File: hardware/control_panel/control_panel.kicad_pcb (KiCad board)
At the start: 2 copper layers, 70 x 37 mm, 12 parts

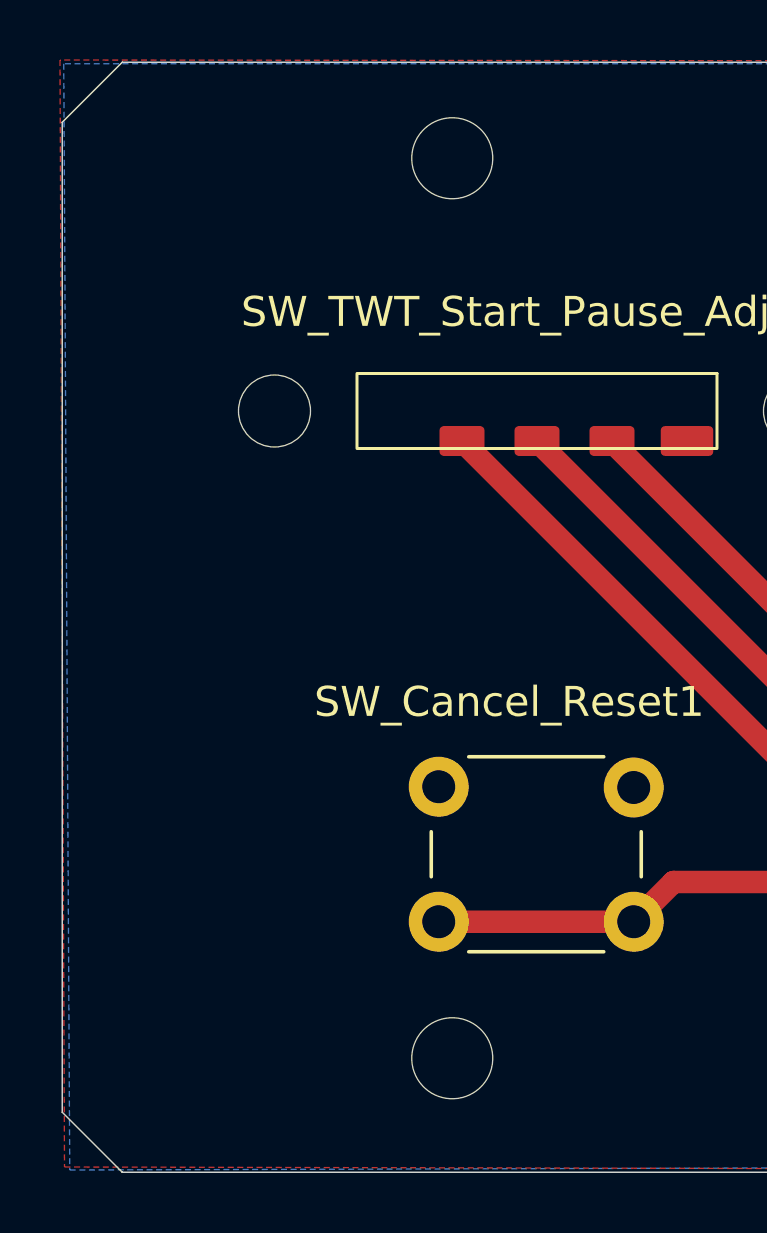
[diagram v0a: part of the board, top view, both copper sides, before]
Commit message: KiCad changes for mountholes
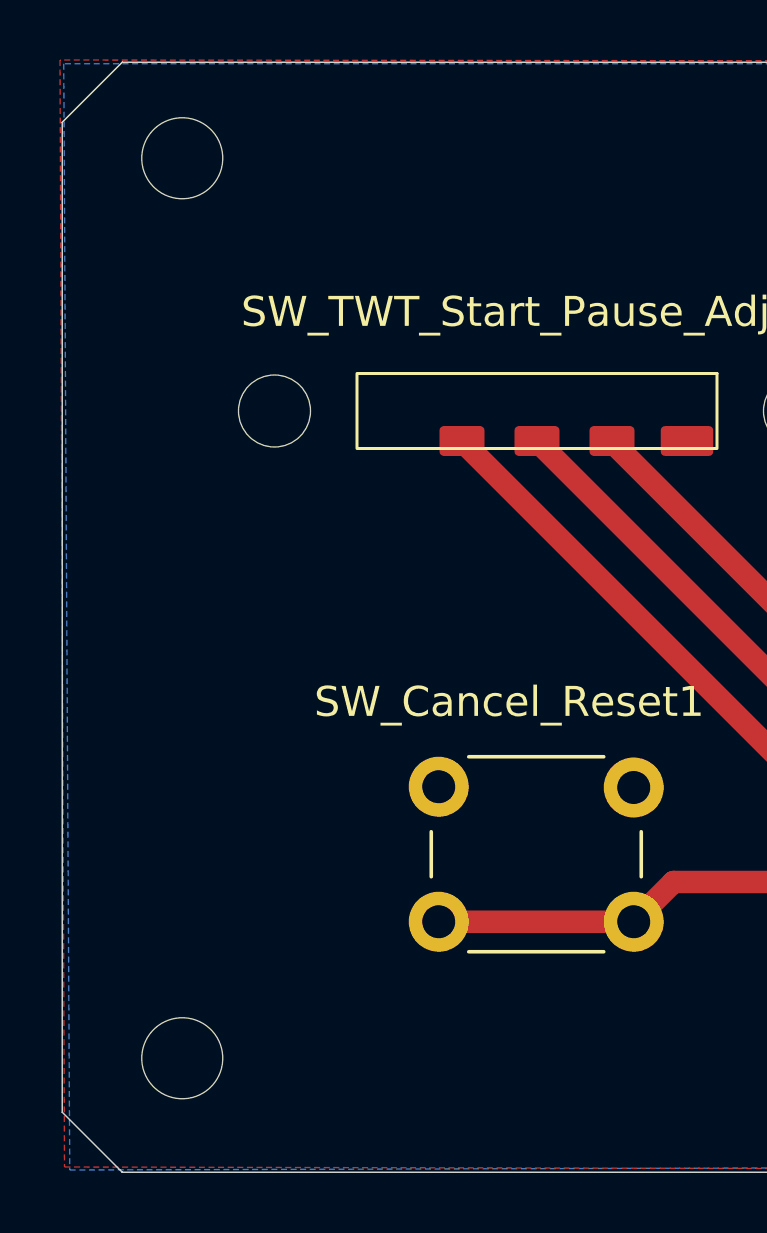
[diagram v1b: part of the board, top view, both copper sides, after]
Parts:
- moved REF** 9.00 mm to (54.0, 53.2)
- moved REF** 9.00 mm to (54.0, 83.2)
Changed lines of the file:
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@@
 	(footprint "MountingHole:MountingHole_2.7mm_M2.5_DIN965"
 		(layer "F.Cu")
-		(at 63 53.2)
+		(at 54 53.2)
 		(descr "Mounting Hole 2.7mm, M2.5, no annular, generated by kicad-footprint-generator mountinghole.py")
 		(tags "mountinghole M2.5 DIN965")
@@
 	(footprint "MountingHole:MountingHole_2.7mm_M2.5_DIN965"
 		(layer "F.Cu")
-		(at 63 83.2)
+		(at 54 83.2)
 		(descr "Mounting Hole 2.7mm, M2.5, no annular, generated by kicad-footprint-generator mountinghole.py")
 		(tags "mountinghole M2.5 DIN965")
@@
 		(min_thickness 0.25)
 		(filled_areas_thickness no)
-		(fill yes
+		(fill
 			(thermal_gap 0.5)
 			(thermal_bridge_width 0.5)
@@
 		(min_thickness 0.25)
 		(filled_areas_thickness no)
-		(fill yes
+		(fill
 			(thermal_gap 0.5)
 			(thermal_bridge_width 0.5)
